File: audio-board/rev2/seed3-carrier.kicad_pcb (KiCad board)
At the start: 4 copper layers, 90 x 56.5 mm, 54 parts, among them J1 NRJ4HF, J2 SJ3-35063AG, J3 DISPLAY_UART, J4 SJ3-35063AG, J5 NRJ4HF, J6 LINE_OUT, J7 POWER_BOARD, Q1 AO3401A, Q2 2N7002, U1 TLV9061IDBVR, U2 TPA6132A2RTE

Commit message: Add a pad after the guitar buffer for active pickups
U1 at unity gain could swing ~4.8 Vpp into AUDIO_IN_1, past the Daisy
pin's 3.6 Vpp full scale and +-1.8 V absolute maximum. R20 (470 ohm,
C4502) into R21 (1k to GND, C4410) scales U1's swing so the pin never
sees more than 3.4 Vpp, even with no module load and U1 at both rails.

The input is now clean to ~4.8 Vpp at J1, which covers passive and
typical 9 V active pickups; hotter sources clip harmlessly in U1.
Passive pickups lose 3.9 dB of converter signal-to-noise. R20/R21 sit
above U1 pin 1 on the board.

DESIGN.md, TEST_PLAN.md (new 1.21b and 5.19), CHANGES.md and the sheet
note are updated. One more extended part (C4502).

Co-Authored-By: Claude Opus 5.5 <noreply@anthropic.com>
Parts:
- added R20: 470, Resistor_SMD:R_1206_3216Metric_Pad1.30x1.75mm_HandSolder, F.Cu at (134.6, 84.0)
- added R21: 1k, Resistor_SMD:R_1206_3216Metric_Pad1.30x1.75mm_HandSolder, F.Cu at (138.4, 84.0)
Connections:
- U1 pad 1: /AUDIO_IN_1 -> Net-(U1A--)
- U1 pad 4: /AUDIO_IN_1 -> Net-(U1A--)

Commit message: Lower the line-out impedance: R11 to 1k, C16 to 3.3 nF
R11 is the line out's output impedance. At 3.3k it cost 2.7 dB into a
10k input and more into lower-impedance gear. At 1k it costs 0.9 dB,
and a shorted J5 still leaves the Daisy at 1k, above its 600 ohm
minimum load. C16 goes to 3.3 nF to keep the 48 kHz corner.

R11 reuses the basic 1k (C4410). JLC had no 3.3 nF C0G 1206 in stock,
so C16 is the 0805 FH 0805CG332J500NT (C486355, extended), placed
where the 1206 was. DESIGN.md, TEST_PLAN.md, CHANGES.md and the sheet
note carry the new values.

Co-Authored-By: Claude Opus 5.5 <noreply@anthropic.com>
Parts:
- C16: value 1nF -> 3.3nF; footprint Capacitor_SMD:C_1206_3216Metric_Pad1.33x1.80mm_HandSolder -> Capacitor_SMD:C_0805_2012Metric_Pad1.18x1.45mm_HandSolder
- R11: value 3.3k -> 1k
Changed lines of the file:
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@@
 		)
 	)
-	(footprint "Capacitor_SMD:C_1206_3216Metric_Pad1.33x1.80mm_HandSolder"
+	(footprint "Capacitor_SMD:C_0805_2012Metric_Pad1.18x1.45mm_HandSolder"
 		(layer "F.Cu")
-		(at 168 72.6)
-		(descr "Capacitor SMD 1206 (3216 Metric), square (rectangular) end terminal, IPC-7351 nominal with elongated pad for handsoldering. (Body size source: IPC-SM-782 page 76, https://www.pcb-3d.com/wordpress/wp-content/uploads/ipc-sm-782a_amendment_1_and_2.pdf)")
+		(at 168 72.6 0)
+		(descr "Capacitor SMD 0805 (2012 Metric), square (rectangular) end terminal, IPC-7351 nominal with elongated pad for handsoldering. (Body size source: IPC-SM-782 page 76, https://www.pcb-3d.com/wordpress/wp-content/uploads/ipc-sm-782a_amendment_1_and_2.pdf, https://docs.google.com/spreadsheets/d/1BsfQQcO9C6DZCsRaXUlFlo91Tg2WpOkGARC1WS5S8t0/edit?usp=sharing)")
 		(tags "capacitor handsolder")
 		(property "Reference" "C16"
-			(at 0 -1.7 0)
+			(at 0 -1.65 0)
 			(layer "F.SilkS")
 			(effects
@@
 			)
 		)
-		(property "Value" "1nF"
-			(at 0 1.85 0)
+		(property "Value" "3.3nF"
+			(at 0 1.68 0)
 			(layer "F.Fab")
 			(effects
@@
 			)
 		)
-		(property "LCSC" "C1885"
+		(property "LCSC" "C486355"
 			(at 0 0 0)
 			(layer "F.Fab")
@@
 		(duplicate_pad_numbers_are_jumpers no)
 		(fp_line
-			(start -0.711252 -0.91)
-			(end 0.711252 -0.91)
+			(start -0.261252 -0.735)
+			(end 0.261252 -0.735)
 			(stroke
 				(width 0.12)
@@
 		)
 		(fp_line
-			(start -0.711252 0.91)
-			(end 0.711252 0.91)
+			(start -0.261252 0.735)
+			(end 0.261252 0.735)
 			(stroke
 				(width 0.12)
@@
 		)
 		(fp_rect
-			(start -2.48 -1.15)
-			(end 2.48 1.15)
+			(start -1.88 -0.98)
+			(end 1.88 0.98)
 			(stroke
 				(width 0.05)
@@
 		)
 		(fp_rect
-			(start -1.6 -0.8)
-			(end 1.6 0.8)
+			(start -1 -0.625)
+			(end 1 0.625)
 			(stroke
 				(width 0.1)
@@
 			(effects
 				(font
-					(size 0.8 0.8)
-					(thickness 0.12)
+					(size 0.5 0.5)
+					(thickness 0.08)
 				)
 			)
 		)
 		(pad "1" smd roundrect
-			(at -1.5625 0)
-			(size 1.325 1.8)
+			(at -1.0375 0 0)
+			(size 1.175 1.45)
 			(layers "F.Cu" "F.Mask" "F.Paste")
-			(roundrect_rratio 0.188679)
+			(roundrect_rratio 0.212766)
 			(net "/LINE_OUT")
 			(pintype "passive")
 		)
 		(pad "2" smd roundrect
-			(at 1.5625 0)
-			(size 1.325 1.8)
+			(at 1.0375 0 0)
+			(size 1.175 1.45)
 			(layers "F.Cu" "F.Mask" "F.Paste")
-			(roundrect_rratio 0.188679)
+			(roundrect_rratio 0.212766)
 			(net "GND")
 			(pintype "passive")
 		)
 		(embedded_fonts no)
-		(model "${KICAD10_3DMODEL_DIR}/Capacitor_SMD.3dshapes/C_1206_3216Metric.step"
+		(model "${KICAD10_3DMODEL_DIR}/Capacitor_SMD.3dshapes/C_0805_2012Metric.step"
 			(offset
 				(xyz 0 0 0)
@@
 			)
 		)
-		(property "Value" "3.3k"
+		(property "Value" "1k"
 			(at 0 1.83 0)
 			(layer "F.Fab")
@@
 			)
 		)
-		(property "LCSC" "C26032"
+		(property "LCSC" "C4410"
 			(at 0 0 180)
 			(layer "F.Fab")

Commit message: Add a 0 ohm jumper in the line out as a DC-block option
The line out has no coupling cap and assumes Daisy pin 19 sits at 0 V
DC, which TEST_PLAN 5.16 has yet to confirm. R22 (0 ohm, C17888, basic)
now sits between the R11/C16 filter and LINE_OUT. If the pin carries
DC, R22 is swapped for a 10 uF 1206 ceramic without a respin; R12 then
holds LINE_OUT at 0 V and the corner with a 10k load is ~1.8 Hz.

R22 sits below R11, left of R12, on the board. DESIGN.md, TEST_PLAN.md,
CHANGES.md and the sheet note point at R22 instead of "fit a cap".

Co-Authored-By: Claude Opus 5.5 <noreply@anthropic.com>
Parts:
- added R22: 0, Resistor_SMD:R_1206_3216Metric_Pad1.30x1.75mm_HandSolder, F.Cu at (163.8, 77.6)
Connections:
- C16 pad 1: /LINE_OUT -> Net-(C16-Pad1)
- R11 pad 2: /LINE_OUT -> Net-(C16-Pad1)
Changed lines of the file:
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@@
 	(footprint "Resistor_SMD:R_1206_3216Metric_Pad1.30x1.75mm_HandSolder"
 		(layer "F.Cu")
+		(at 163.83 77.6 -90)
+		(descr "Resistor SMD 1206 (3216 Metric), square (rectangular) end terminal, IPC-7351 nominal with elongated pad for handsoldering. (Body size source: IPC-SM-782 page 72, https://www.pcb-3d.com/wordpress/wp-content/uploads/ipc-sm-782a_amendment_1_and_2.pdf)")
+		(tags "resistor handsolder")
+		(property "Reference" "R22"
+			(at -3.45 0 0)
+			(layer "F.SilkS")
+			(effects
+				(font
+					(size 0.8 0.8)
+					(thickness 0.12)
+				)
+			)
+		)
+		(property "Value" "0"
+			(at 0 1.83 -90)
+			(layer "F.Fab")
+			(effects
+				(font
+					(size 1 1)
+					(thickness 0.15)
+				)
+			)
+		)
+		(property "Datasheet" ""
+			(at 0 0 -90)
+			(layer "F.Fab")
+			(hide yes)
+			(effects
+				(font
+					(size 1.27 1.27)
+				)
+			)
+		)
+		(property "Description" "Resistor, small US symbol"
+			(at 0 0 -90)
+			(layer "F.Fab")
+			(hide yes)
+			(effects
+				(font
+					(size 1.27 1.27)
+				)
+			)
+		)
+		(property "KiLib_Generator" "SMD_2terminal_chip_molded"
+			(at 0 0 -90)
+			(layer "F.Fab")
+			(hide yes)
+			(effects
+				(font
+					(size 1 1)
+					(thickness 0.15)
+				)
+			)
+		)
+		(property "LCSC" "C17888"
+			(at 0 0 0)
+			(layer "F.Fab")
+			(hide yes)
+			(effects
+				(font
+					(size 1.27 1.27)
+					(thickness 0.15)
+				)
+			)
+		)
+		(property ki_fp_filters "R_*")
+		(sheetname "/")
+		(sheetfile "seed3-carrier.kicad_sch")
+		(units
+			(unit
+				(name "A")
+				(pins "1" "2")
+			)
+		)
+		(attr smd)
+		(duplicate_pad_numbers_are_jumpers no)
+		(fp_line
+			(start -0.727064 -0.91)
+			(end 0.727064 -0.91)
+			(stroke
+				(width 0.12)
+				(type solid)
+			)
+			(layer "F.SilkS")
+		)
+		(fp_line
+			(start -0.727064 0.91)
+			(end 0.727064 0.91)
+			(stroke
+				(width 0.12)
+				(type solid)
+			)
+			(layer "F.SilkS")
+		)
+		(fp_rect
+			(start -2.45 -1.13)
+			(end 2.45 1.13)
+			(stroke
+				(width 0.05)
+				(type solid)
+			)
+			(fill no)
+			(layer "F.CrtYd")
+		)
+		(fp_rect
+			(start -1.6 -0.8)
+			(end 1.6 0.8)
+			(stroke
+				(width 0.1)
+				(type solid)
+			)
+			(fill no)
+			(layer "F.Fab")
+		)
+		(fp_text user "${REFERENCE}"
+			(at 0 0 -90)
+			(layer "F.Fab")
+			(effects
+				(font
+					(size 0.8 0.8)
+					(thickness 0.12)
+				)
+			)
+		)
+		(pad "1" smd roundrect
+			(at -1.55 0 -90)
+			(size 1.3 1.75)
+			(layers "F.Cu" "F.Mask" "F.Paste")
+			(roundrect_rratio 0.192308)
+			(net "Net-(C16-Pad1)")
+			(pintype "passive")
+		)
+		(pad "2" smd roundrect
+			(at 1.55 0 -90)
+			(size 1.3 1.75)
+			(layers "F.Cu" "F.Mask" "F.Paste")
+			(roundrect_rratio 0.192308)
+			(net "/LINE_OUT")
+			(pintype "passive")
+		)
+		(embedded_fonts no)
+		(model "${KICAD10_3DMODEL_DIR}/Resistor_SMD.3dshapes/R_1206_3216Metric.step"
+			(offset
+				(xyz 0 0 0)
+			)
+			(scale
+				(xyz 1 1 1)
+			)
+			(rotate
+				(xyz 0 0 0)
+			)
+		)
+	)
+	(footprint "Resistor_SMD:R_1206_3216Metric_Pad1.30x1.75mm_HandSolder"
+		(layer "F.Cu")
 		(at 134.62 84.0 90)
 		(descr "Resistor SMD 1206 (3216 Metric), square (rectangular) end terminal, IPC-7351 nominal with elongated pad for handsoldering. (Body size source: IPC-SM-782 page 72, https://www.pcb-3d.com/wordpress/wp-content/uploads/ipc-sm-782a_amendment_1_and_2.pdf)")
@@
 			(layers "F.Cu" "F.Mask" "F.Paste")
 			(roundrect_rratio 0.212766)
-			(net "/LINE_OUT")
+			(net "Net-(C16-Pad1)")
 			(pintype "passive")
 		)
@@
 			(layers "F.Cu" "F.Mask" "F.Paste")
 			(roundrect_rratio 0.192308)
-			(net "/LINE_OUT")
+			(net "Net-(C16-Pad1)")
 			(pintype "passive")
 		)

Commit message: Add ESD diodes on every jack signal contact
D1-D6 (Nexperia PESD5V0S1BA, SOD-323, C19224) clamp J1 tip, J2
tip/ring, J4 tip/ring and J5 tip to GND, each placed beside its jack.
Bidirectional with a 5 V working voltage, so no audio signal on these
contacts reaches it; 5 nA leakage and 35 pF don't load the 1 MOhm
guitar input. The isolated J2/J4 detect switches need none.

The sheet gains a JACK ESD PROTECTION section, with the power-board
block shifted left to make room, and the J1/J2 nets are named
GTR_TIP, AUX_TIP and AUX_RING. DESIGN.md also records that the J2/J4
footprint matches the Same Sky datasheet layout; TEST_PLAN adds 1.21c.

Co-Authored-By: Claude Opus 5.5 <noreply@anthropic.com>
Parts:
- added D1: PESD5V0S1BA, Diode_SMD:D_SOD-323, F.Cu at (120.8, 85.7)
- added D2: PESD5V0S1BA, Diode_SMD:D_SOD-323, F.Cu at (134.6, 98.0)
- added D3: PESD5V0S1BA, Diode_SMD:D_SOD-323, F.Cu at (120.8, 99.5)
- added D4: PESD5V0S1BA, Diode_SMD:D_SOD-323, F.Cu at (168.6, 99.0)
- added D5: PESD5V0S1BA, Diode_SMD:D_SOD-323, F.Cu at (154.6, 97.8)
- added D6: PESD5V0S1BA, Diode_SMD:D_SOD-323, F.Cu at (169.6, 91.0)
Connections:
- net Net-(C1-Pad1) renamed /GTR_TIP
- net Net-(J2-R) renamed /AUX_RING
- net Net-(J2-T) renamed /AUX_TIP

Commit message: Drop the 1/4" line out, the input pad, R22 and D6
The speaker send now goes only to the internal header (J5, was J6), and the
power board connector is J6 (was J7). R20 stays as a 470 ohm series resistor
with no pad, since active pickups are out of scope. Docs and test plan follow.

Co-Authored-By: Claude Opus 5.5 <noreply@anthropic.com>
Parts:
- removed D6: PESD5V0S1BA, Diode_SMD:D_SOD-323
- removed the J5 at (184.9, 89.5)
- removed R21: 1k, Resistor_SMD:R_1206_3216Metric_Pad1.30x1.75mm_HandSolder
- removed R22: 0, Resistor_SMD:R_1206_3216Metric_Pad1.30x1.75mm_HandSolder
- C1: footprint Capacitor_SMD:C_1206_3216Metric_Pad1.33x1.80mm_HandSolder -> Capacitor_SMD:C_0805_2012Metric_Pad1.18x1.45mm_HandSolder
- C10, C11: footprint Capacitor_SMD:C_1210_3225Metric_Pad1.33x2.70mm_HandSolder -> Capacitor_SMD:C_0805_2012Metric_Pad1.18x1.45mm_HandSolder
- R10, R20, R5: footprint Resistor_SMD:R_1206_3216Metric_Pad1.30x1.75mm_HandSolder -> Resistor_SMD:R_0805_2012Metric_Pad1.20x1.40mm_HandSolder
- renumbered J6 to J5, J7 to J6
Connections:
- C16 pad 1: Net-(C16-Pad1) -> /LINE_OUT
- R11 pad 2: Net-(C16-Pad1) -> /LINE_OUT

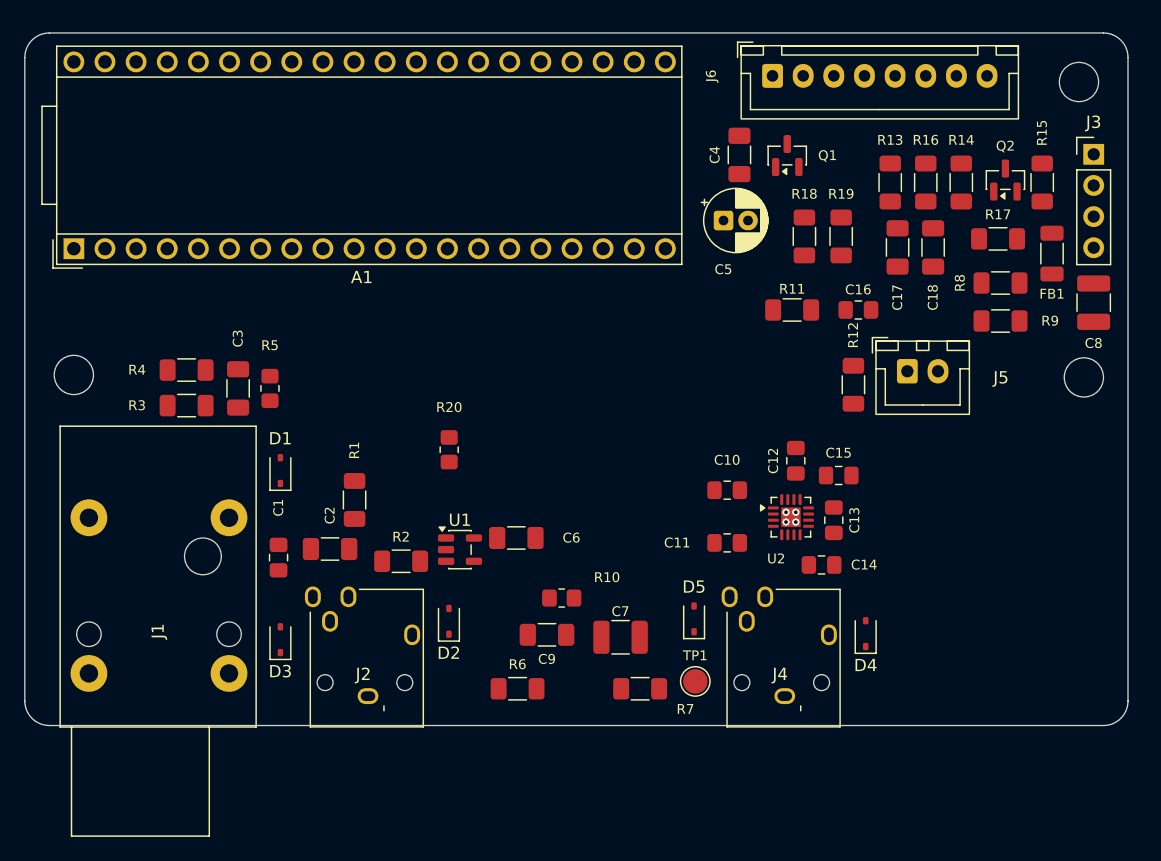
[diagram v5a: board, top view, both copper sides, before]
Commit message: Re-place the carrier passives and route the analog section
Each filter and divider now sits at its load, so long runs are the
low-impedance ones: the AUX sum moves under Daisy pin 17 (J2 moves right
so its lines no longer cross the guitar row), R10/C9 join U2's input caps,
and the VREF divider sits at R1. U2 is rotated 180 degrees so OUTL and SGND
run side by side on L1 to J4's tip and sleeve; OUTR takes one via to L4.
J5 moves into the power corner so the power board's ground loop through
J5/J6 stays away from U1 and U2.

Every SMD GND pad gets its own via. The guitar row, AUX and headphone
paths, speaker send, U1/U2 decoupling, power entry and an analog-only +5V
branch on L4 are routed. HP_DETECT moves from Daisy pin 34 to pin 23,
which sits above the headphone section. DRC is clean apart from the
existing jack-overhang silk warnings.

Co-Authored-By: Claude Opus 5.5 <noreply@anthropic.com>
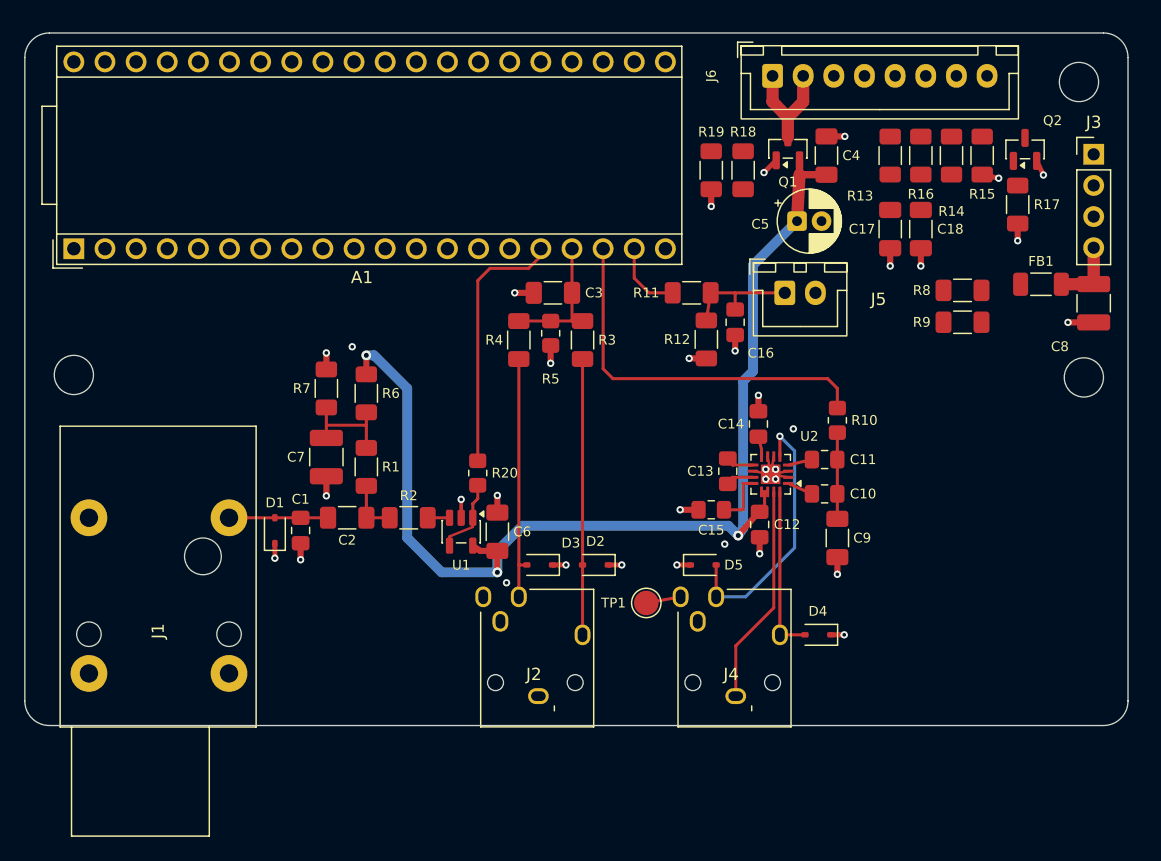
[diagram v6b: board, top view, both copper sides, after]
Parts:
- moved R7 35.4 mm to (124.6, 79.0), turned to 90 degrees
- moved R3 32.7 mm to (145.5, 75.0), turned to 90 degrees
- moved C7 28.1 mm to (124.6, 84.6), turned to 90 degrees
- moved R4 27.2 mm to (140.3, 75.0), turned to 90 degrees
- moved R6 27.1 mm to (127.9, 79.4), turned to -90 degrees
- moved C3 26.8 mm to (143.1, 71.2), turned to 180 degrees
- moved R10 26.8 mm to (166.3, 81.6), turned to 90 degrees
- moved C9 25.0 mm to (166.3, 91.2), turned to -90 degrees
- moved R5 23.3 mm to (142.9, 74.5)
- moved D3 22.0 mm to (142.0, 93.4), turned to 180 degrees
- moved J2 13.9 mm to (141.9, 104.1)
- moved D2 12.8 mm to (146.6, 93.4), turned to 180 degrees
- moved C14 12.6 mm to (159.8, 81.9), turned to 90 degrees
- moved R12 12.6 mm to (155.6, 75.0)
- moved R19 11.9 mm to (156.0, 61.2), turned to -90 degrees
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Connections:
- A1 pad 23: unconnected-(A1-ADC_1-Pad23) -> /HP_DETECT
- A1 pad 34: /HP_DETECT -> unconnected-(A1-SAI2_FS-Pad34)
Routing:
- net +5V: track 0.00 -> 92.1 mm, vias 0 -> 3
- net GND: track 0.00 -> 59.4 mm, vias 4 -> 35
- net /AUDIO_OUT_1: track 0.00 -> 31.2 mm
- net /AUX_TIP: track 0.00 -> 22.5 mm
- net /HP_R: track 0.00 -> 21.9 mm, vias 0 -> 1
- net /AUDIO_IN_1: track 0.00 -> 21.3 mm
- net /AUX_RING: track 0.00 -> 20.0 mm
- net /HP_L: track 0.00 -> 13.7 mm
- net /AUDIO_IN_2: track 0.00 -> 11.1 mm
- net /LINE_OUT: track 0.00 -> 9.69 mm
- net /5V_IN: track 0.00 -> 9.42 mm
- net /VREF: track 0.00 -> 8.65 mm
- net /GTR_TIP: track 0.00 -> 8.08 mm
- net /HP_SOURCE: track 0.00 -> 7.04 mm
- net Net-(U1A--): track 0.00 -> 6.37 mm
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
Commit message: Move C8 off the board edge and enlarge references to 1.0 mm
JLC's assembly terms need 2.5 mm between a part body and the board edge,
and C8 was 1.5 mm from the right edge. FB1 now sits beside J3 pin 4 and
C8 lies horizontally below them, 3.35 mm from the edge; DISPLAY_5V and
C8's GND via are re-routed to match.

References go from 0.8 mm / 0.12 mm to JLC's legibility minimum of
1.0 mm / 0.15 mm. To fit them, the power board series resistors move
1.6 mm down from J6 with labels alternating above and below, C18 and
R8/R9 shift to clear the new labels, and Q1's GND via moves clear of
Q1's label.

Checked with tools/kicad/board_check.py: no JLC errors and no text-size
warnings remain; only the deferred routing (22 connections) is open.

Co-Authored-By: Claude Opus 5.5 <noreply@anthropic.com>
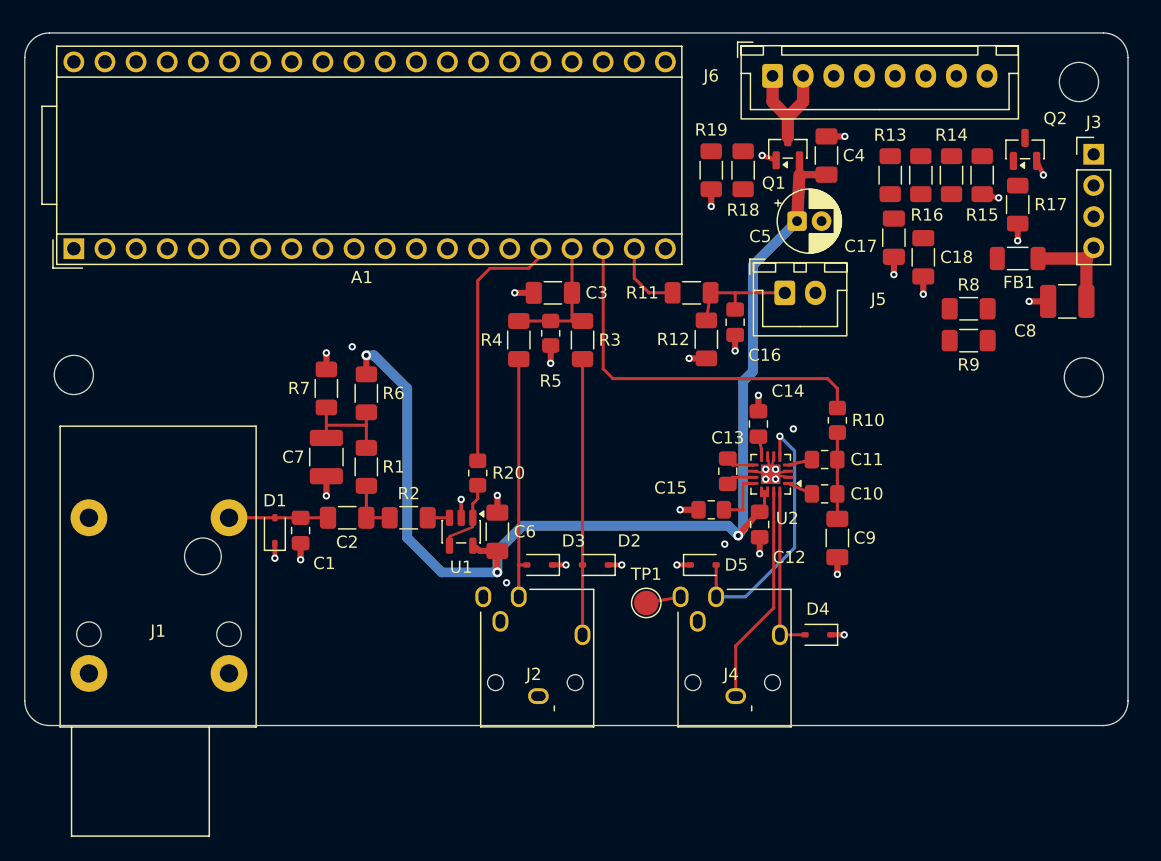
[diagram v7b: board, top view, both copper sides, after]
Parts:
- moved FB1 2.83 mm to (181.0, 68.4)
- moved C18 2.31 mm to (173.3, 68.3)
- moved C8 2.16 mm to (185.1, 71.9), turned to 180 degrees
- moved R13 1.60 mm to (170.6, 61.6)
- moved R14 1.60 mm to (175.6, 61.6)
- moved R15 1.60 mm to (178.1, 61.6)
- moved R16 1.60 mm to (173.1, 61.6)
- moved R8 1.58 mm to (177.0, 72.5)
- moved R9 1.58 mm to (177.0, 75.1)
- moved C17 0.76 mm to (170.9, 66.7)
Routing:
- net /DISPLAY_5V: track 5.61 -> 8.51 mm
- net GND: track 59.4 -> 58.6 mm
